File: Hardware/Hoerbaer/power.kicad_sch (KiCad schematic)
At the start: 78 parts, among them J12 VExt 5V, J13 TS, J14 Battery 1S Li-Ion, J15 Battery 1S Li-Ion, U10 TPS63001, U11 TPS61288, U14 TPS22810DRV, U8 BQ24073RGT, U9 MAX17048G

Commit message: BOM FIxes
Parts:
- C18, C24, C25, C26, C33, C34: LCSC C458949 -> C1525; MPN MT15B104K160CT -> CL05B104KO5NNNC
- C29: LCSC C1517770 -> C84705; MPN GCM155L81H472KA37D -> CL05B472KB5NNNC
- C30, C31: LCSC C386133 -> C86287; MPN UMK105CG270JV-F -> CL05C270JB5NNNC
- D11, D5, D7: LCSC C432789 -> C122867; MPN S54BF -> SS54BF
- J13: now not fitted
- R68: value 90kΩ -> 91kΩ; LCSC C114151 -> C327323; MPN RC0402FR-07140KL -> RC0402FR-0791KL
- U14: LCSC (none) -> C527679; MPN (none) -> TPS22810DRVR
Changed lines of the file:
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@@
 			)
 		)
-		(property "LCSC" "C386133"
+		(property "LCSC" "C86287"
 			(at 237.49 110.49 0)
 			(effects
@@
 			)
 		)
-		(property "MPN" "UMK105CG270JV-F"
+		(property "MPN" "CL05C270JB5NNNC"
 			(at 237.49 110.49 0)
 			(effects
@@
 			)
 		)
-		(property "LCSC" "C458949"
+		(property "LCSC" "C1525"
 			(at 182.88 102.87 0)
 			(effects
@@
 			)
 		)
-		(property "MPN" "MT15B104K160CT"
+		(property "MPN" "CL05B104KO5NNNC"
 			(at 182.88 102.87 0)
 			(effects
@@
 			)
 		)
-		(property "LCSC" "C458949"
+		(property "LCSC" "C1525"
 			(at 185.42 38.1 0)
 			(effects
@@
 			)
 		)
-		(property "MPN" "MT15B104K160CT"
+		(property "MPN" "CL05B104KO5NNNC"
 			(at 185.42 38.1 0)
 			(effects
@@
 			)
 		)
+		(property "LCSC" "C527679"
+			(at 255.27 62.23 0)
+			(effects
+				(font
+					(size 1.27 1.27)
+				)
+			)
+		)
+		(property "MPN" "TPS22810DRVR"
+			(at 255.27 62.23 0)
+			(effects
+				(font
+					(size 1.27 1.27)
+				)
+			)
+		)
 		(pin "6"
 		)
@@
 			)
 		)
-		(property "Value" "90kΩ"
+		(property "Value" "91kΩ"
 			(at 245.11 92.71 0)
 			(effects
@@
 			)
 		)
-		(property "LCSC" "C114151"
+		(property "LCSC" "C327323"
 			(at 243.84 91.44 0)
 			(effects
@@
 			)
 		)
-		(property "MPN" "RC0402FR-07140KL "
+		(property "MPN" "RC0402FR-0791KL "
 			(at 243.84 91.44 0)
 			(effects
@@
 			)
 		)
-		(property "LCSC" "C458949"
+		(property "LCSC" "C1525"
 			(at 199.39 93.98 0)
 			(effects
@@
 			)
 		)
-		(property "MPN" "MT15B104K160CT"
+		(property "MPN" "CL05B104KO5NNNC"
 			(at 199.39 93.98 0)
 			(effects
@@
 			)
 		)
-		(property "LCSC" "C1517770"
+		(property "LCSC" "C84705"
 			(at 233.68 107.95 0)
 			(effects
@@
 			)
 		)
-		(property "MPN" "GCM155L81H472KA37D"
+		(property "MPN" "CL05B472KB5NNNC"
 			(at 233.68 107.95 0)
 			(effects
@@
 			)
 		)
-		(property "LCSC" "C458949"
+		(property "LCSC" "C1525"
 			(at 74.93 146.05 0)
 			(effects
@@
 			)
 		)
-		(property "MPN" "MT15B104K160CT"
+		(property "MPN" "CL05B104KO5NNNC"
 			(at 74.93 146.05 0)
 			(effects
@@
 			)
 		)
-		(property "MPN" "S54BF"
+		(property "MPN" "SS54BF"
 			(at 96.52 44.45 0)
 			(effects
@@
 			)
 		)
-		(property "LCSC" "C432789"
+		(property "LCSC" "C122867"
 			(at 96.52 44.45 0)
 			(effects
@@
 			)
 		)
-		(property "LCSC" "C386133"
+		(property "LCSC" "C86287"
 			(at 250.19 101.6 0)
 			(effects
@@
 			)
 		)
-		(property "MPN" "UMK105CG270JV-F"
+		(property "MPN" "CL05C270JB5NNNC"
 			(at 250.19 101.6 0)
 			(effects
@@
 			)
 		)
-		(property "LCSC" "C458949"
+		(property "LCSC" "C1525"
 			(at 266.7 67.31 0)
 			(effects
@@
 			)
 		)
-		(property "MPN" "MT15B104K160CT"
+		(property "MPN" "CL05B104KO5NNNC"
 			(at 266.7 67.31 0)
 			(effects
@@
 		(in_bom yes)
 		(on_board yes)
-		(dnp no)
+		(dnp yes)
 		(property "Reference" "J13"
 			(at 138.43 143.51 0)
@@
 			)
 		)
-		(property "MPN" "S54BF"
+		(property "MPN" "SS54BF"
 			(at 86.36 44.45 0)
 			(effects
@@
 			)
 		)
-		(property "LCSC" "C432789"
+		(property "LCSC" "C122867"
 			(at 86.36 44.45 0)
 			(effects
@@
 			)
 		)
-		(property "MPN" "S54BF"
+		(property "MPN" "SS54BF"
 			(at 76.2 44.45 0)
 			(effects
@@
 			)
 		)
-		(property "LCSC" "C432789"
+		(property "LCSC" "C122867"
 			(at 76.2 44.45 0)
 			(effects
@@
 			)
 		)
-		(property "LCSC" "C458949"
+		(property "LCSC" "C1525"
 			(at 238.76 62.23 0)
 			(effects
@@
 			)
 		)
-		(property "MPN" "MT15B104K160CT"
+		(property "MPN" "CL05B104KO5NNNC"
 			(at 238.76 62.23 0)
 			(effects

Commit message: Production
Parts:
- J13: FT Rotation Offset (none) -> 90; JLCPCB Rotation Offset 90 -> (none)
- U11: FT Position Offset (none) -> 0.0,0.474
- U9: FT Rotation Offset (none) -> 270; JLCPCB Rotation Offset 90 -> (none)
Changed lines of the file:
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@@
 		(on_board yes)
 		(dnp no)
-		(fields_autoplaced yes)
 		(property "Reference" "U14"
 			(at 255.27 53.34 0)
@@
 					(size 1.27 1.27)
 				)
+				(hide yes)
 			)
 		)
 		(property "MPN" "TPS22810DRVR"
-			(at 255.27 62.23 0)
+			(at 255.778 62.992 0)
 			(effects
 				(font
 					(size 1.27 1.27)
 				)
+				(hide yes)
 			)
 		)
@@
 			)
 		)
-		(property "JLCPCB Rotation Offset" "90"
-			(at 102.87 149.86 0)
-			(effects
-				(font
-					(size 1.27 1.27)
-				)
-				(hide yes)
-			)
-		)
 		(property "Check_prices" ""
 			(at 102.87 149.86 0)
@@
 			)
 		)
+		(property "FT Rotation Offset" "270"
+			(at 102.87 149.86 0)
+			(effects
+				(font
+					(size 1.27 1.27)
+				)
+			)
+		)
 		(pin "1"
 		)
@@
 			)
 		)
+		(property "FT Position Offset" "0.0,0.474"
+			(at 213.36 105.41 0)
+			(effects
+				(font
+					(size 1.27 1.27)
+				)
+				(hide yes)
+			)
+		)
 		(pin "1"
 		)
@@
 			)
 		)
-		(property "JLCPCB Rotation Offset" "90"
-			(at 140.97 142.24 0)
-			(effects
-				(font
-					(size 1.27 1.27)
-				)
-				(hide yes)
-			)
-		)
 		(property "Check_prices" ""
 			(at 140.97 142.24 0)
@@
 			(at 140.97 142.24 0)
 			(effects
+				(font
+					(size 1.27 1.27)
+				)
+			)
+		)
+		(property "FT Rotation Offset" "90"
+			(at 140.97 142.24 0)
+			(effects

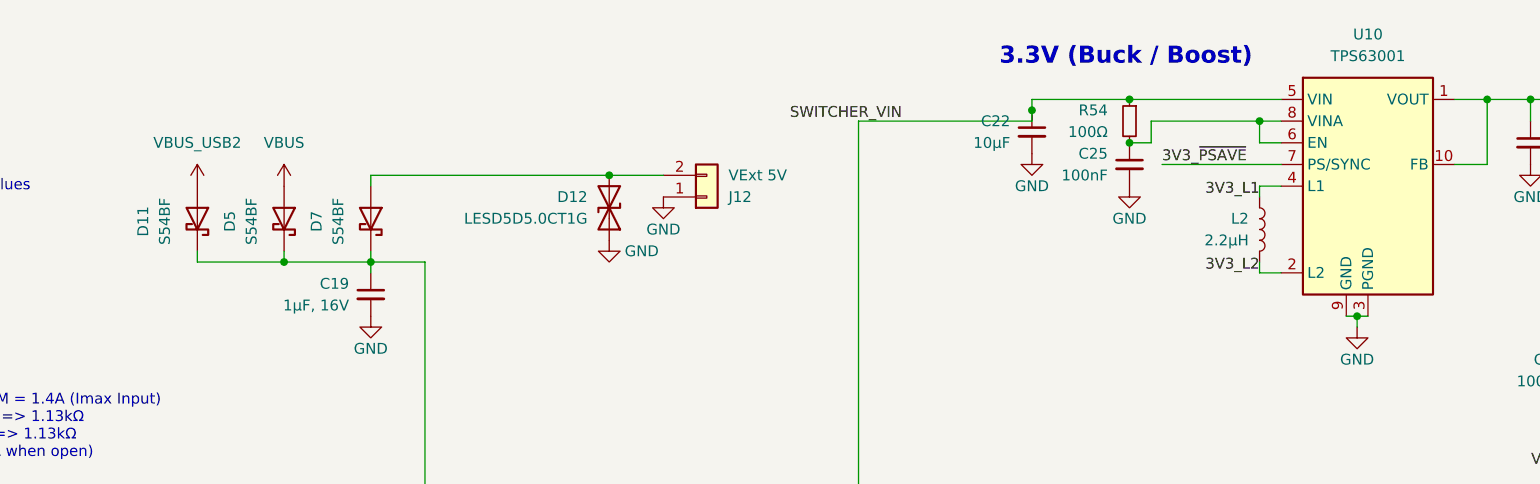
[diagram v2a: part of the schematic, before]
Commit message: Layout fixes (production feedback)
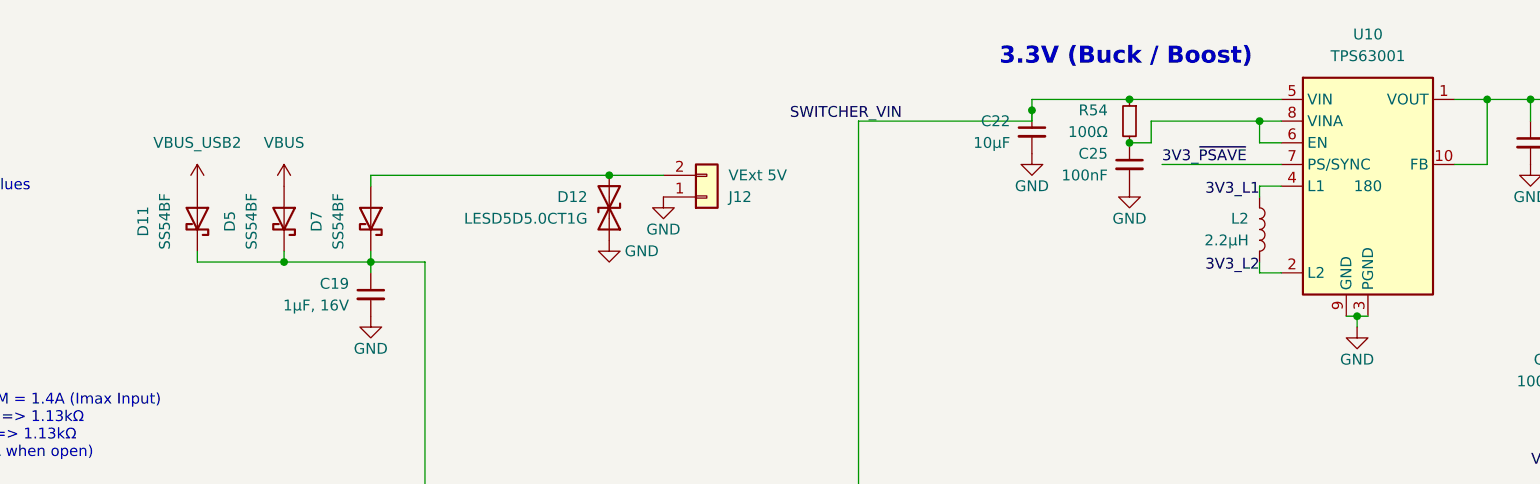
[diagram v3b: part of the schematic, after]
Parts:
- D11, D5, D7: value S54BF -> SS54BF; footprint Baer_Footprints:S54BF -> Baer_Footprints:SS54BF
- U10: FT Rotation Offset (none) -> 180
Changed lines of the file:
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@@
 			)
 		)
-		(property "Value" "S54BF"
+		(property "Value" "SS54BF"
 			(at 92.71 44.7675 0)
 			(effects
@@
 			)
 		)
-		(property "Footprint" "Baer_Footprints:S54BF"
+		(property "Footprint" "Baer_Footprints:SS54BF"
 			(at 96.52 44.45 0)
 			(effects
@@
 			)
 		)
-		(property "Datasheet" "~"
+		(property "Datasheet" "https://jlcpcb.com/api/file/downloadByFileSystemAccessId/8586195341142339584"
 			(at 96.52 44.45 0)
 			(effects
@@
 			)
 		)
-		(property "Value" "S54BF"
+		(property "Value" "SS54BF"
 			(at 82.55 44.7675 0)
 			(effects
@@
 			)
 		)
-		(property "Footprint" "Baer_Footprints:S54BF"
+		(property "Footprint" "Baer_Footprints:SS54BF"
 			(at 86.36 44.45 0)
 			(effects
@@
 			)
 		)
-		(property "Datasheet" "~"
+		(property "Datasheet" "https://jlcpcb.com/api/file/downloadByFileSystemAccessId/8586195341142339584"
 			(at 86.36 44.45 0)
 			(effects
@@
 			)
 		)
-		(property "Value" "S54BF"
+		(property "Value" "SS54BF"
 			(at 72.39 44.7675 0)
 			(effects
@@
 			)
 		)
-		(property "Footprint" "Baer_Footprints:S54BF"
+		(property "Footprint" "Baer_Footprints:SS54BF"
 			(at 76.2 44.45 0)
 			(effects
@@
 			)
 		)
-		(property "Datasheet" "~"
+		(property "Datasheet" "https://jlcpcb.com/api/file/downloadByFileSystemAccessId/8586195341142339584"
 			(at 76.2 44.45 0)
 			(effects
@@
 			(at 213.36 40.64 0)
 			(effects
+				(font
+					(size 1.27 1.27)
+				)
+			)
+		)
+		(property "FT Rotation Offset" "180"
+			(at 213.36 40.64 0)
+			(effects

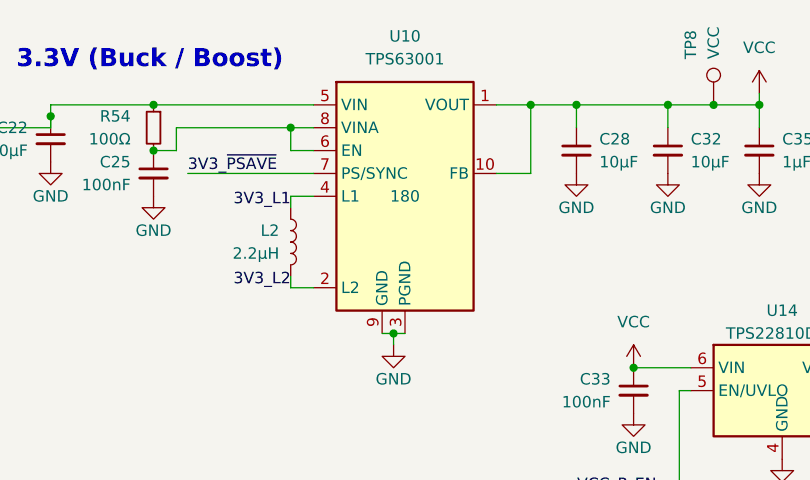
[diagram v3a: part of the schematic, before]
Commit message: Layout fixes, production fixes
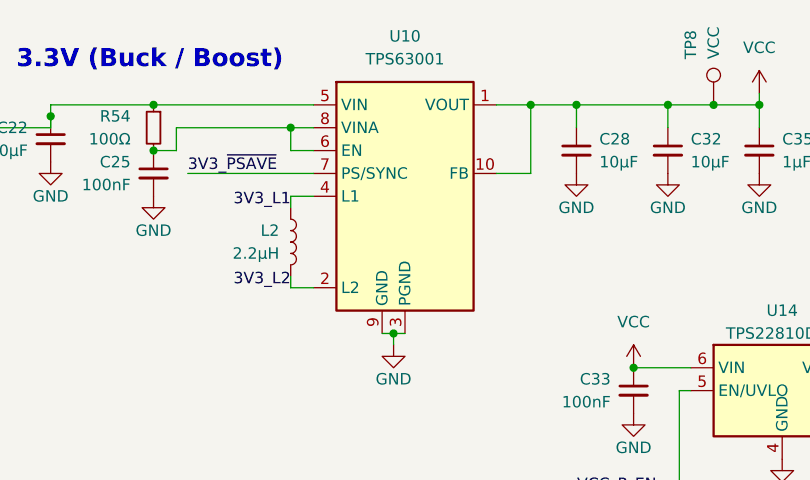
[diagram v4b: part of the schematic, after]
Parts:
- U10: FT Rotation Offset 180 -> (none)
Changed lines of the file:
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@@
 			)
 		)
-		(property "FT Rotation Offset" "180"
+		(property "FT Rotation Offset" ""
 			(at 213.36 40.64 0)
 			(effects
